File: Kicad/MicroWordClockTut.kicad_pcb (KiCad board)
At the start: 2 copper layers, 32.8 x 43.5 mm, 11 parts, among them J1 Conn_01x02_Male, J2 Conn_02x03_Male, SW1 SW_SPST, U1 ATmega328P-AU, U2 8x8_LED_MATRIX, U3 DS1307Z+, U4 8x8_LED_MATRIX, Y1 Crystal

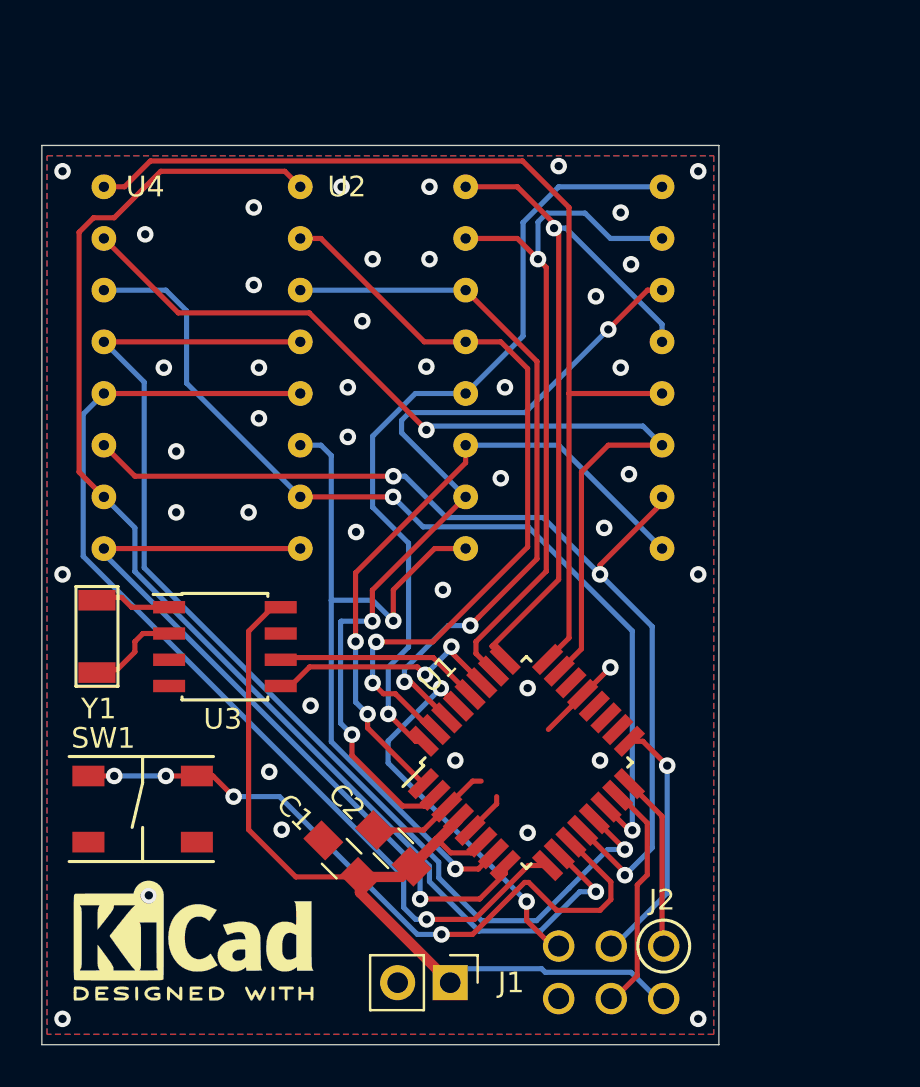
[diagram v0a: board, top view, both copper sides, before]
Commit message: started routing.  it is small.  pinswapped a lot
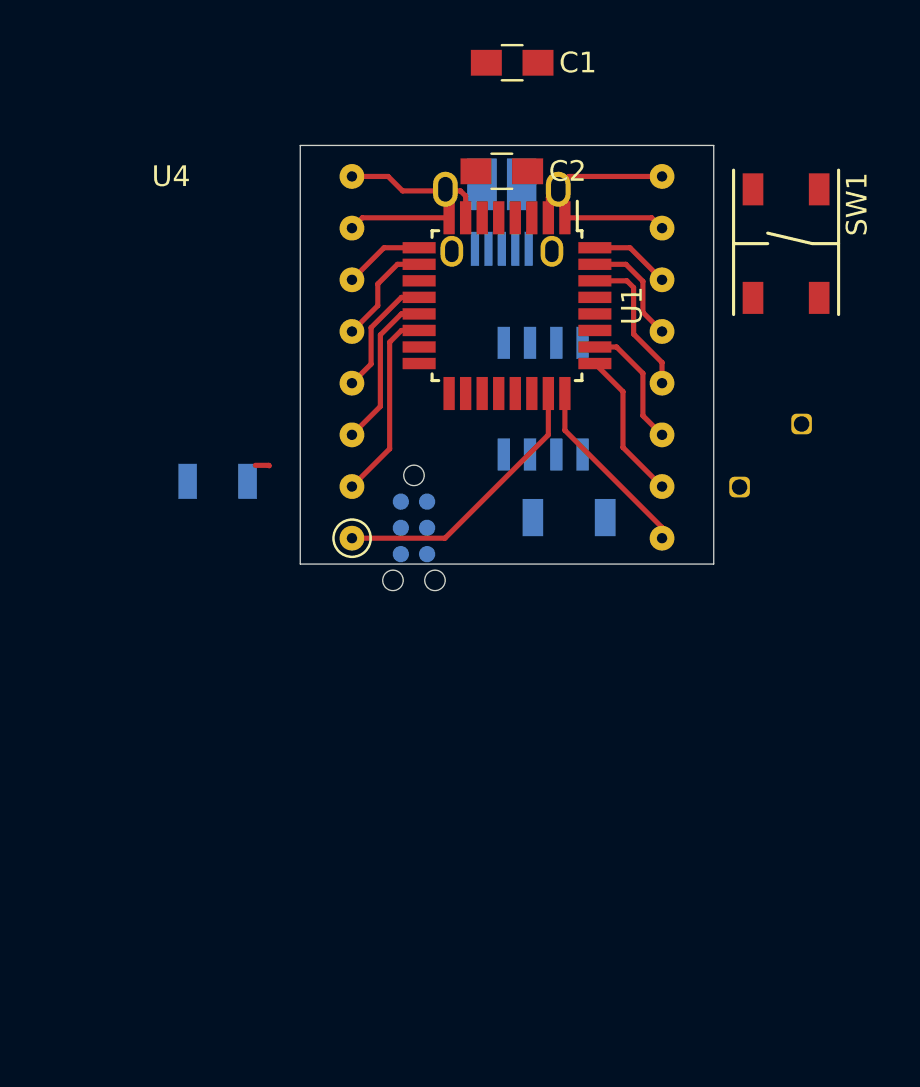
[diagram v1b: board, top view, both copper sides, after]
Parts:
- removed G***: LOGO, MicroWordClockTut:mwkicad
- removed U2: 8x8_LED_MATRIX, MicroWordClockTut:788LEDMATRIX
- added BT1: Battery_Cell, MicroWordClockTut:BR1225VCN, B.Cu at (146.2, 109.5)
- added R1: 200, Resistors_SMD:R_1206, B.Cu at (119.5, 110.8)
- J1: value Conn_01x02_Male -> USB_B_Micro; footprint Connector_PinHeader_2.54mm:PinHeader_1x02_P2.54mm_Vertical -> Connectors:USB_Micro-B_10103594-0001LF; moved to B.Cu
- J2: footprint MicroWordClockTut:2x3 Header -> Connectors:Tag-Connect_TC2030-IDC-NL; moved to B.Cu
- U3, Y1: moved to B.Cu
- moved SW1 41.4 mm to (147.0, 99.2), turned to 270 degrees
- moved C1 39.4 mm to (133.8, 90.5), turned to 0 degrees
- moved J1 37.1 mm to (133.2, 98.0), turned to 0 degrees
- moved C2 33.2 mm to (133.2, 95.8), turned to 0 degrees
- moved Y1 23.5 mm to (136.5, 112.5), turned to 180 degrees
- moved J2 23.5 mm to (129.0, 113.0)
- moved U1 22.1 mm to (133.5, 102.2), turned to 270 degrees
- moved U3 19.5 mm to (135.2, 106.8), turned to 90 degrees
- moved U4 1.35 mm to (133.5, 113.5)
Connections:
- net /R2 renamed /14
- J1 pad 2: GND -> Net-(J1-Pad2)
- U1 pad 1: /C5 -> /1
- U1 pad 10: /C4 -> /10
- U1 pad 12: /C6 -> /12
- U1 pad 13: /C1 -> /13
- U1 pad 2: /R6 -> /2
- U1 pad 23: /C7 -> /23
- U1 pad 24: /C8 -> /24
- U1 pad 25: /R5 -> /25
- U1 pad 26: /R7 -> /26
- U1 pad 30: /C2 -> /30
- U1 pad 31: /C3 -> /31
- U1 pad 32: /R8 -> /32
- U1 pad 7: /R3 -> /7
- U1 pad 8: /R1 -> /8
- U1 pad 9: /R4 -> /9
- U3 pad 3: (no net) -> Net-(BT1-Pad1)
- U4 pad C1: /C1 -> /10
- U4 pad C2: /C2 -> /9
- U4 pad C3: /C3 -> /8
- U4 pad C4: /C4 -> /7
- U4 pad C5: /C5 -> /24
- U4 pad C6: /C6 -> /25
- U4 pad C7: /C7 -> /26
- U4 pad C8: /C8 -> /30
- U4 pad R1: /R1 -> /23
- U4 pad R3: /R3 -> /13
- U4 pad R4: /R4 -> /12
- U4 pad R5: /R5 -> /31
- U4 pad R6: /R6 -> /32
- U4 pad R7: /R7 -> /1
- U4 pad R8: /R8 -> /2
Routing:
- net /C4: track 63.1 -> 0.00 mm, vias 1 -> 0
- net /C1: track 55.5 -> 0.00 mm, vias 1 -> 0
- net /C8: track 50.7 -> 0.00 mm
- net /C6: track 50.7 -> 0.00 mm, vias 3 -> 0
- net /R4: track 49.5 -> 0.00 mm, vias 1 -> 0
- net /C7: track 45.8 -> 0.00 mm, vias 1 -> 0
- net +5V: track 44.7 -> 0.00 mm
- net /R6: track 41.6 -> 0.00 mm, vias 3 -> 0
- net /R8: track 39.0 -> 0.00 mm, vias 1 -> 0
- net /R1: track 37.8 -> 0.00 mm, vias 1 -> 0
- net /C3: track 37.5 -> 0.00 mm, vias 2 -> 0
- net /14: track 45.8 -> 9.40 mm, vias 2 -> 0
- net /R5: track 36.0 -> 0.00 mm, vias 1 -> 0
- net /R3: track 35.6 -> 0.00 mm, vias 2 -> 0
- net /C2: track 34.4 -> 0.00 mm, vias 2 -> 0
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- removed copper zone on B.Cu, net GND
- removed copper zone on F.Cu, net GND
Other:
- board size 32.8 x 43.5 mm -> 20 x 20.2 mm

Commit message: latest version with tiny switch NanoT
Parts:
- removed R1: 200, Resistors_SMD:R_1206
- C1: moved to B.Cu
- J1: footprint Connectors:USB_Micro-B_10103594-0001LF -> MicroWordClockTut:10118192-0001LF
- J2: footprint Connectors:Tag-Connect_TC2030-IDC-NL -> MicroWordClockTut:side connector; moved to F.Cu
- SW1: value SW_SPST -> SW_SPST_2PIN; footprint MicroWordClockTut:PTS647 tact switch -> MicroWordClockTut:NanoT BS
- moved SW1 23.1 mm to (124.0, 101.2)
- moved BT1 12.8 mm to (133.5, 111.0), turned to 0 degrees
- moved C1 10.1 mm to (132.2, 100.5)
- moved Y1 9.17 mm to (138.2, 103.5), turned to 270 degrees
- moved J2 5.03 mm to (133.6, 115.0), turned to 180 degrees
- moved U3 3.61 mm to (132.2, 104.8), turned to 180 degrees
- moved J1 2.02 mm to (133.5, 96.0)
- moved C2 0.50 mm to (133.8, 95.8)
- moved U1 0.35 mm to (133.8, 102.0)
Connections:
- J1 pad 2: Net-(J1-Pad2) -> (no net)
- J1 pad 3: Net-(J1-Pad3) -> (no net)
- J2 pad 1: /MISO -> /RST
- J2 pad 4: /MOSI -> /MISO
- J2 pad 5: /RST -> /MOSI
- SW1 pad 2: Net-(SW1-Pad1) -> GND
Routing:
- net +5V: track 0.00 -> 20.5 mm, vias 0 -> 2
- net /RST: track 0.00 -> 17.7 mm, vias 0 -> 1
- net GND: track 0.00 -> 14.0 mm, vias 0 -> 3
- net /MOSI: track 0.00 -> 12.3 mm, vias 0 -> 1
- net /SDA: track 0.00 -> 11.9 mm, vias 0 -> 1
- net /SCK: track 0.00 -> 11.4 mm, vias 0 -> 1
- net /MISO: track 0.00 -> 11.0 mm, vias 0 -> 1
- net /SCL: track 0.00 -> 10.6 mm, vias 0 -> 1
- net Net-(SW1-Pad1): track 0.00 -> 7.16 mm, vias 0 -> 2
- net Net-(BT1-Pad1): track 0.00 -> 5.98 mm
- net Net-(U3-Pad2): track 0.00 -> 3.77 mm
- net Net-(U3-Pad1): track 0.00 -> 3.75 mm
- net /24: track 8.95 -> 10.2 mm
- net /10: track 5.21 -> 5.97 mm
- net Net-(J1-Pad2): track 0.69 -> 0.00 mm
- added copper zone on B.Cu, net GND
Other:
- board size 20 x 20.2 mm -> 20.5 x 20.5 mm
- rule trace_min: 0.2 -> 0.15
- rule via_min_drill: 0.3 -> 0.254

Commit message: this version released to osh park
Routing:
- net /23: track 13.9 -> 15.1 mm
- net /SCK: track 11.4 -> 10.5 mm
- net Net-(SW1-Pad1): track 7.16 -> 6.33 mm
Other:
- board text added: "5V"
- board text added: "G"
- board text added: "MISO"
- board text added: "MOSI"
- board text added: "SCK"
- board text added: "~RST"
